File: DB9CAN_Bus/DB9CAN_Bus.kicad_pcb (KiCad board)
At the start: 2 copper layers, 14 parts, among them J1 DE9_Receptacle, J10 DE9_Receptacle, J2 DE9_Receptacle, J3 DE9_Receptacle, J4 DE9_Receptacle, J5 DE9_Receptacle, J6 DE9_Receptacle, J7 DE9_Receptacle, J8 DE9_Receptacle, J9 DE9_Receptacle

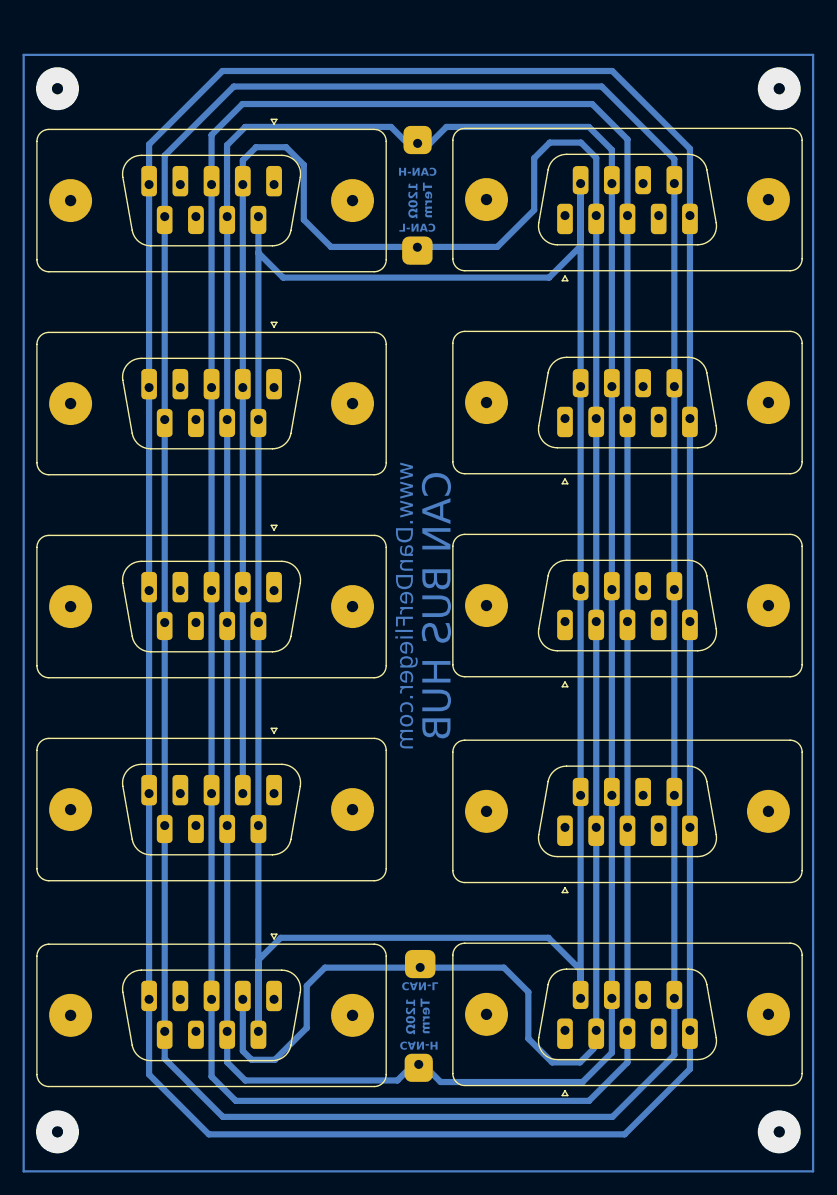
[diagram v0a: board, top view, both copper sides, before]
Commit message: Split the AOA LED project into two projects - one for the LEDs and one for the Nano board and the MCP2515 CAN board.
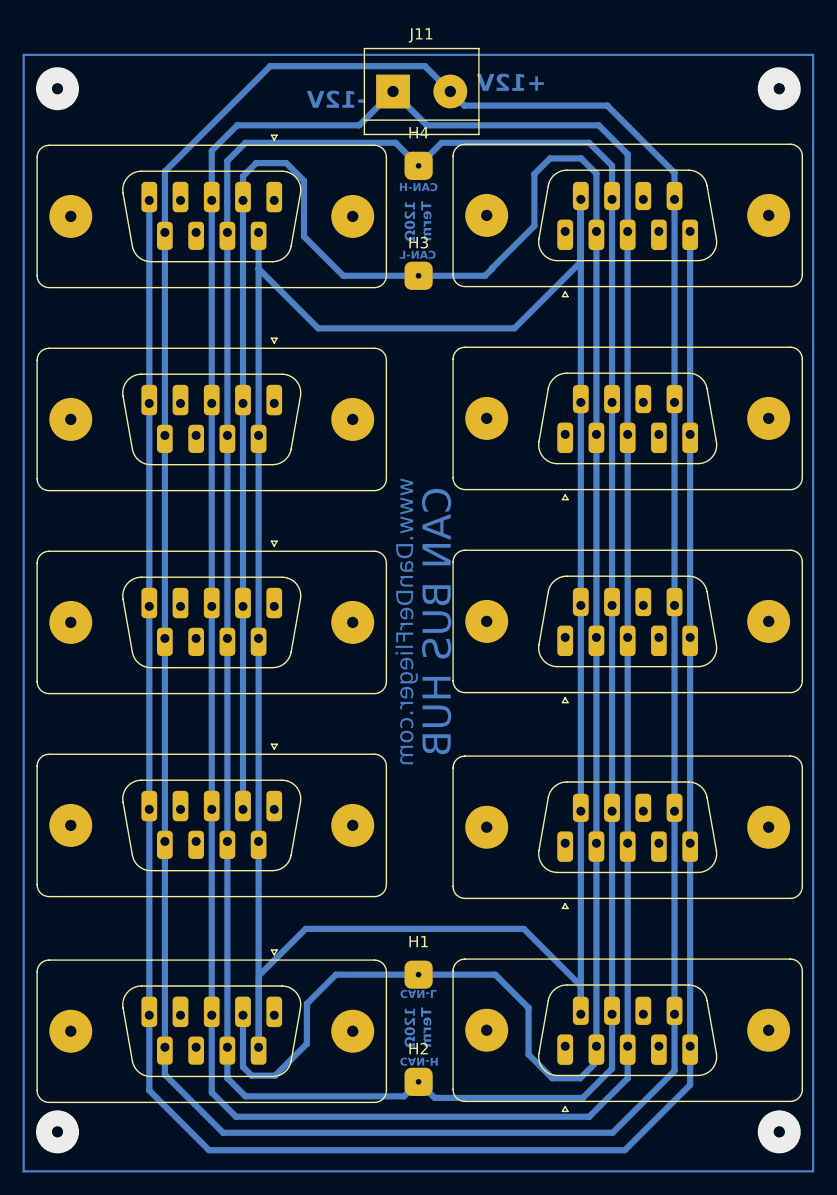
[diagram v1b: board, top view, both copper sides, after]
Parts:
- removed ? (x4): , 
- added H1: MountingHole_Pad, MountingHole:MountingHole_2.2mm_M2_DIN965_Pad, F.Cu at (85.0, 131.6)
- added H2: MountingHole_Pad, MountingHole:MountingHole_2.2mm_M2_DIN965_Pad, F.Cu at (85.0, 141.1)
- added H3: MountingHole_Pad, MountingHole:MountingHole_2.2mm_M2_DIN965_Pad, F.Cu at (85.0, 69.6)
- added H4: MountingHole_Pad, MountingHole:MountingHole_2.2mm_M2_DIN965_Pad, F.Cu at (85.0, 59.8)
- added J11: Screw_Terminal_01x02, TerminalBlock:TerminalBlock_bornier-2_P5.08mm, F.Cu at (82.8, 53.2)
- moved J1 1.41 mm to (72.2, 62.9)
- moved J10 1.41 mm to (98.0, 65.7)
- moved J2 1.41 mm to (72.2, 80.9)
- moved J3 1.41 mm to (72.2, 98.9)
- moved J4 1.41 mm to (72.2, 116.9)
- moved J7 1.41 mm to (98.0, 119.9)
- moved J8 1.41 mm to (98.0, 101.7)
- moved J9 1.41 mm to (98.0, 83.7)
- moved J5 1.41 mm to (72.2, 135.2)
- moved J6 1.41 mm to (98.0, 137.9)
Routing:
- net Net-(J1-Pad5): track 270.2 -> 207.2 mm
- net Net-(J1-Pad6): track 220.4 -> 224.7 mm
- net Net-(J11-Pin_2): track 259.5 -> 262.3 mm
- net Net-(J11-Pin_1): track 243.9 -> 246.0 mm
- net Net-(H1-Pad1): track 227.0 -> 228.5 mm
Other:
- board text added: "+12V"
- board text added: "-12V"
